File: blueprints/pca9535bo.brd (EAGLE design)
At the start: 160 x 100 mm, 8 parts, among them IC1 PCA9535D, J1 0R, J2 0R, J3 0R

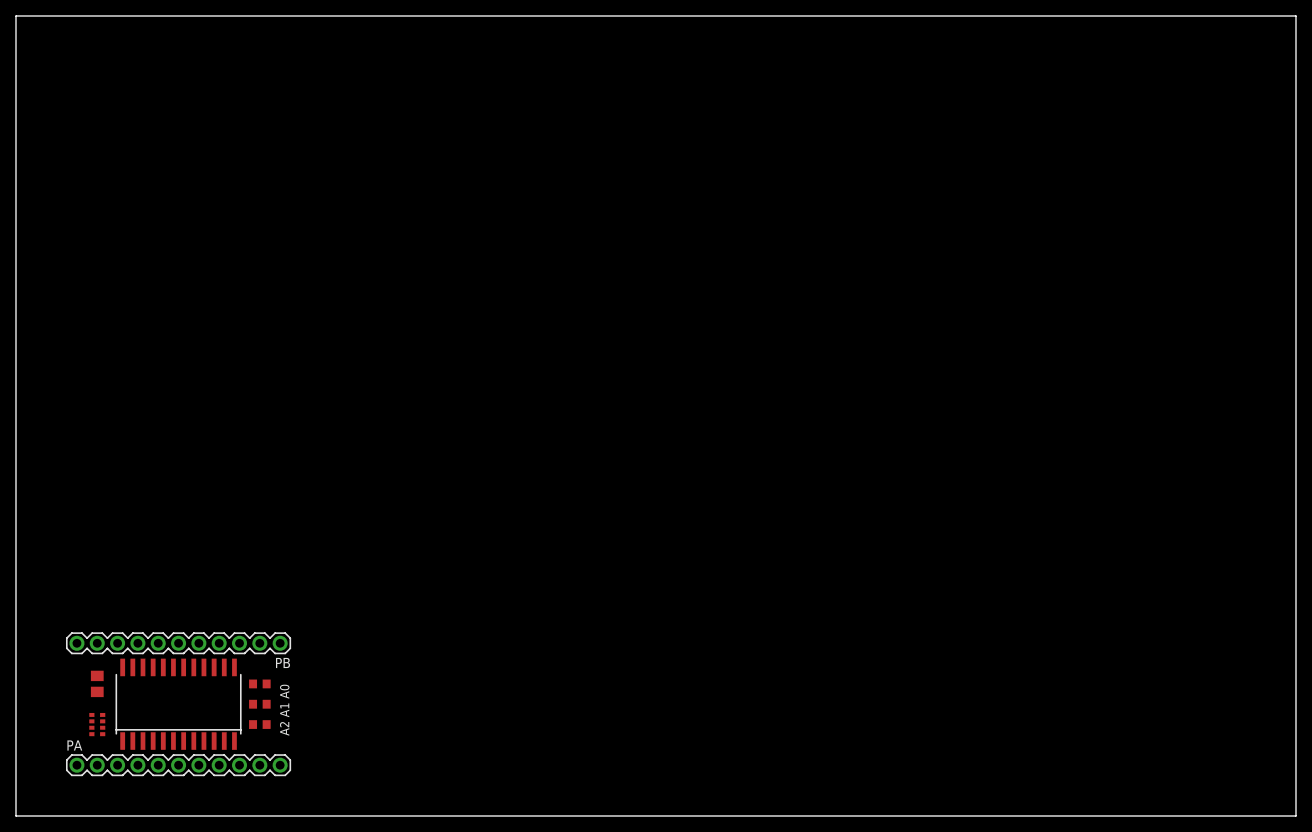
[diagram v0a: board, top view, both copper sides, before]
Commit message: I2C pullups and sizing down
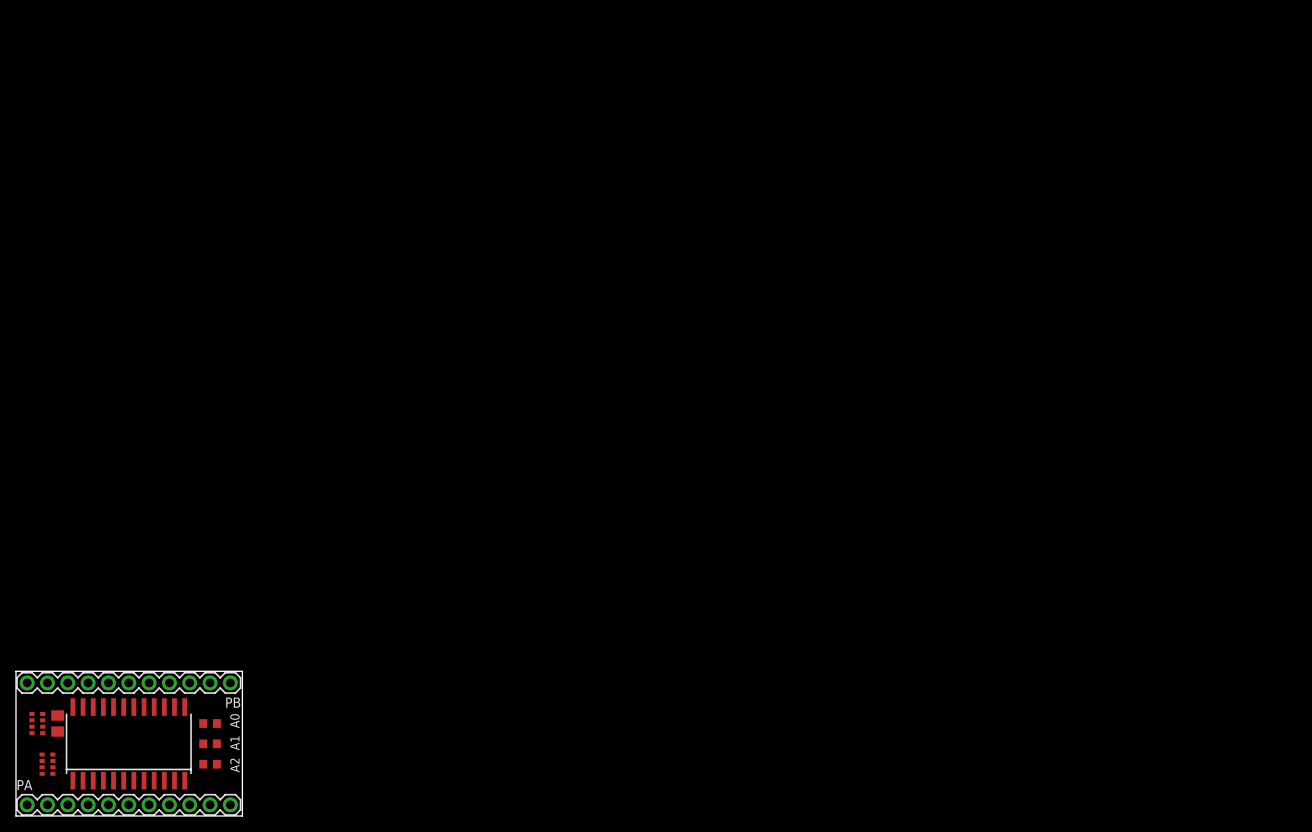
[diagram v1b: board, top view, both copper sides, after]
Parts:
- added PU2: 4.7k, resistor-dil:CAY16
- moved IC1 7.95 mm to (14.1, 9.02)
- moved J1 7.95 mm to (24.3, 11.6)
- moved J3 7.95 mm to (24.3, 9.02)
- moved PB 7.95 mm to (26.8, 16.6)
- moved PA 7.95 mm to (1.40, 1.40)
- moved PU 7.95 mm to (3.94, 6.48)
- moved J2 7.95 mm to (24.3, 6.48)
- moved C1 7.00 mm to (5.21, 11.6)
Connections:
- net 5V: now also PU2.1, PU2.4
- net SCL: now also PU2.5, PU2.6
- net SDA: now also PU2.7, PU2.8
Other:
- board size 160 x 100 mm -> 28.3 x 18.1 mm

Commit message: ground polygons
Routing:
- added copper zone on layer 1, net GND
- added copper zone on layer 16, net GND
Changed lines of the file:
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@@
 <contactref element="IC1" pad="8"/>
 <contactref element="PA" pad="8"/>
-<wire x1="16.002" y1="4.417" x2="19.177" y2="1.397" width="0" layer="19" extent="1-1"/>
+<wire x1="19.177" y1="1.397" x2="16.002" y2="4.417" width="0" layer="19" extent="1-1"/>
 </signal>
 <signal name="PA5">
@@
 <contactref element="IC1" pad="19"/>
 <contactref element="PB" pad="7"/>
-<wire x1="13.462" y1="13.617" x2="11.557" y2="16.637" width="0" layer="19" extent="1-1"/>
+<wire x1="11.557" y1="16.637" x2="13.462" y2="13.617" width="0" layer="19" extent="1-1"/>
 </signal>
 <signal name="PB7">
@@
 <contactref element="PU2" pad="5"/>
 <wire x1="3.937" y1="16.637" x2="9.652" y2="13.617" width="0" layer="19" extent="1-1"/>
-<wire x1="3.342" y1="10.357" x2="9.652" y2="13.617" width="0" layer="19" extent="1-1"/>
-<wire x1="3.342" y1="11.157" x2="3.342" y2="10.357" width="0" layer="19" extent="1-1"/>
+<wire x1="3.342" y1="11.157" x2="3.937" y2="16.637" width="0" layer="19" extent="1-1"/>
+<wire x1="3.342" y1="10.357" x2="3.342" y2="11.157" width="0" layer="19" extent="1-1"/>
 </signal>
 <signal name="SDA">
@@
 <contactref element="PU2" pad="7"/>
 <contactref element="PU2" pad="8"/>
-<wire x1="1.397" y1="16.637" x2="8.382" y2="13.617" width="0" layer="19" extent="1-1"/>
-<wire x1="3.342" y1="11.957" x2="8.382" y2="13.617" width="0" layer="19" extent="1-1"/>
-<wire x1="3.342" y1="12.757" x2="3.342" y2="11.957" width="0" layer="19" extent="1-1"/>
+<wire x1="3.342" y1="12.757" x2="8.382" y2="13.617" width="0" layer="19" extent="1-1"/>
+<wire x1="3.342" y1="11.957" x2="3.342" y2="12.757" width="0" layer="19" extent="1-1"/>
+<wire x1="1.397" y1="16.637" x2="3.342" y2="12.757" width="0" layer="19" extent="1-1"/>
 </signal>
 <signal name="5V">
@@
 <contactref element="PU2" pad="4"/>
 <wire x1="5.207" y1="12.557" x2="7.112" y2="13.617" width="0" layer="19" extent="1-1"/>
-<wire x1="3.262" y1="7.677" x2="5.207" y2="12.557" width="0" layer="19" extent="1-1"/>
+<wire x1="1.992" y1="12.757" x2="5.207" y2="12.557" width="0" layer="19" extent="1-1"/>
+<wire x1="1.992" y1="10.357" x2="1.992" y2="12.757" width="0" layer="19" extent="1-1"/>
+<wire x1="3.262" y1="7.677" x2="1.992" y2="10.357" width="0" layer="19" extent="1-1"/>
 <wire x1="3.262" y1="6.877" x2="3.262" y2="7.677" width="0" layer="19" extent="1-1"/>
 <wire x1="3.262" y1="6.077" x2="3.262" y2="6.877" width="0" layer="19" extent="1-1"/>
 <wire x1="3.262" y1="5.277" x2="3.262" y2="6.077" width="0" layer="19" extent="1-1"/>
 <wire x1="3.937" y1="1.397" x2="3.262" y2="5.277" width="0" layer="19" extent="1-1"/>
-<wire x1="1.992" y1="10.357" x2="3.937" y2="1.397" width="0" layer="19" extent="1-1"/>
-<wire x1="1.992" y1="12.757" x2="1.992" y2="10.357" width="0" layer="19" extent="1-1"/>
 </signal>
 <signal name="GND">
@@
 <contactref element="J2" pad="2"/>
 <contactref element="J3" pad="2"/>
-<wire x1="25.107" y1="9.017" x2="25.107" y2="11.557" width="0" layer="19" extent="1-1"/>
-<wire x1="25.107" y1="6.477" x2="25.107" y2="9.017" width="0" layer="19" extent="1-1"/>
-<wire x1="21.082" y1="4.417" x2="25.107" y2="6.477" width="0" layer="19" extent="1-1"/>
-<wire x1="5.207" y1="10.557" x2="21.082" y2="4.417" width="0" layer="19" extent="1-1"/>
-<wire x1="1.397" y1="1.397" x2="5.207" y2="10.557" width="0" layer="19" extent="1-1"/>
+<polygon width="0.254" layer="16" spacing="0.254" isolate="0.254">
+<vertex x="0" y="18.034"/>
+<vertex x="0" y="0"/>
+<vertex x="28.321" y="0"/>
+<vertex x="28.321" y="18.161"/>
+<vertex x="0" y="18.161"/>
+</polygon>
+<polygon width="0.254" layer="1" spacing="0.254" isolate="0.254">
+<vertex x="0" y="18.034"/>
+<vertex x="0" y="0"/>
+<vertex x="28.321" y="0"/>
+<vertex x="28.321" y="18.034"/>
+</polygon>
 </signal>
 <signal name="A1">

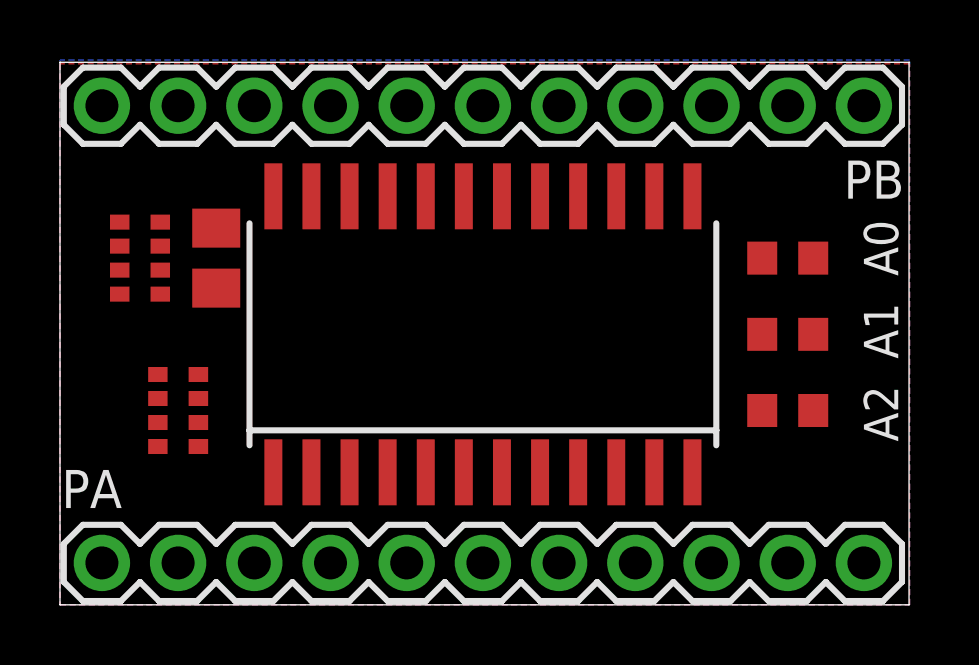
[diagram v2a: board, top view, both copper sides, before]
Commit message: two polygons at least was a bad idea
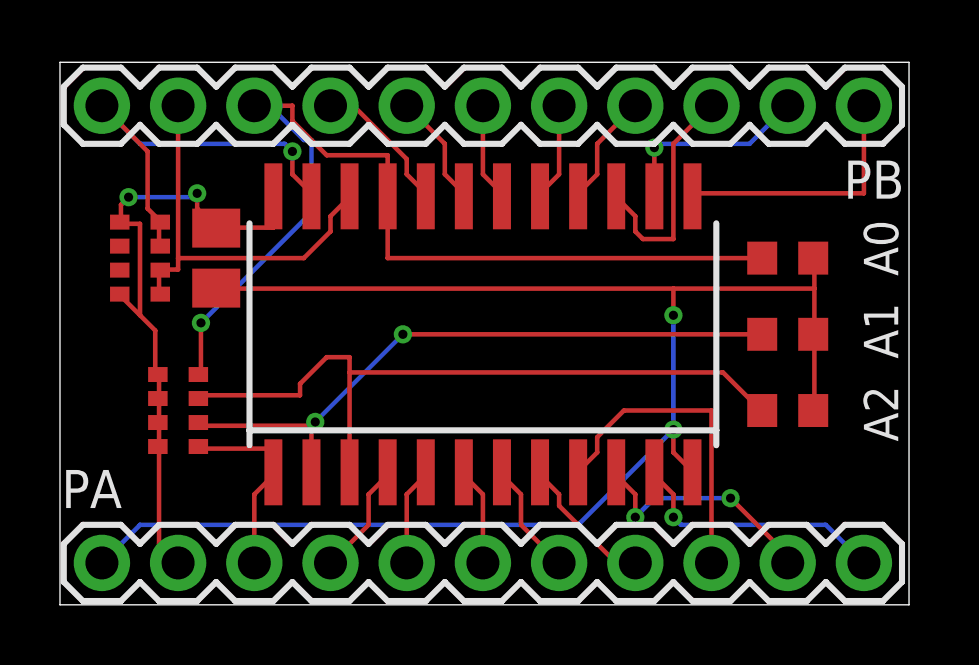
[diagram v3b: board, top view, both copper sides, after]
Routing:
- net GND: track 0.00 -> 52.4 mm, vias 0 -> 2
- net A0: track 0.00 -> 33.1 mm, vias 0 -> 1
- net A2: track 0.00 -> 24.0 mm
- net A1: track 0.00 -> 21.7 mm, vias 0 -> 2
- net 5V: track 0.00 -> 21.3 mm, vias 0 -> 2
- net SDA: track 0.00 -> 14.2 mm, vias 0 -> 1
- net SCL: track 0.00 -> 13.8 mm
- net PA5: track 0.00 -> 10.7 mm
- net PA7: track 0.00 -> 8.74 mm, vias 0 -> 1
- net PB0: track 0.00 -> 8.73 mm
- net PA6: track 0.00 -> 8.15 mm, vias 0 -> 2
- net PB2: track 0.00 -> 7.78 mm
- net PB1: track 0.00 -> 6.65 mm, vias 0 -> 1
- net INT-: track 0.00 -> 6.60 mm
- net PB7: track 0.00 -> 4.78 mm
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- removed copper zone on layer 1, net GND
- removed copper zone on layer 16, net GND

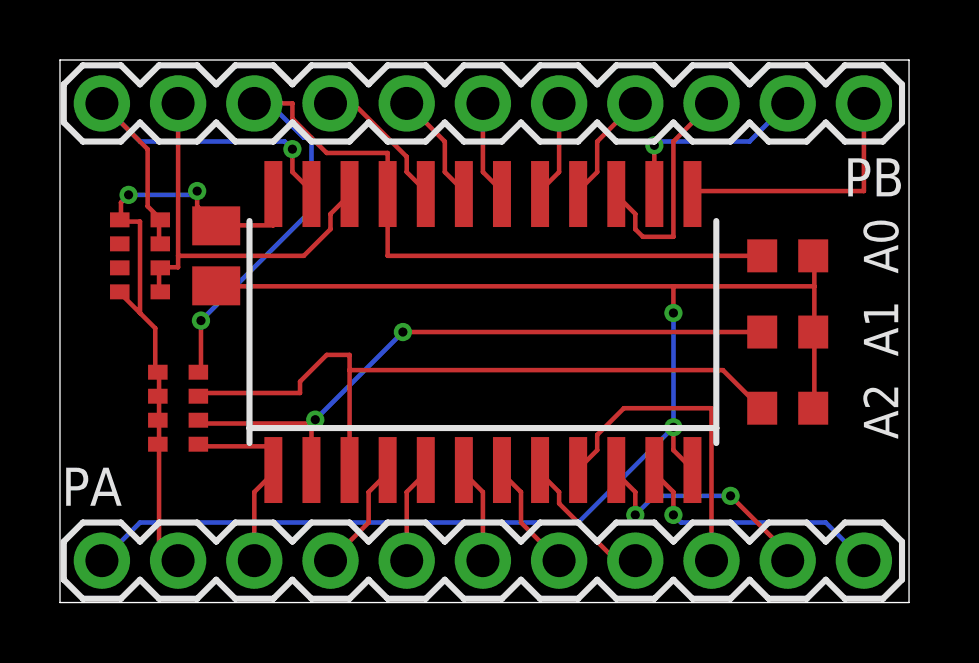
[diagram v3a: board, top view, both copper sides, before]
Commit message: 10mil traces seem to route just fine so use them
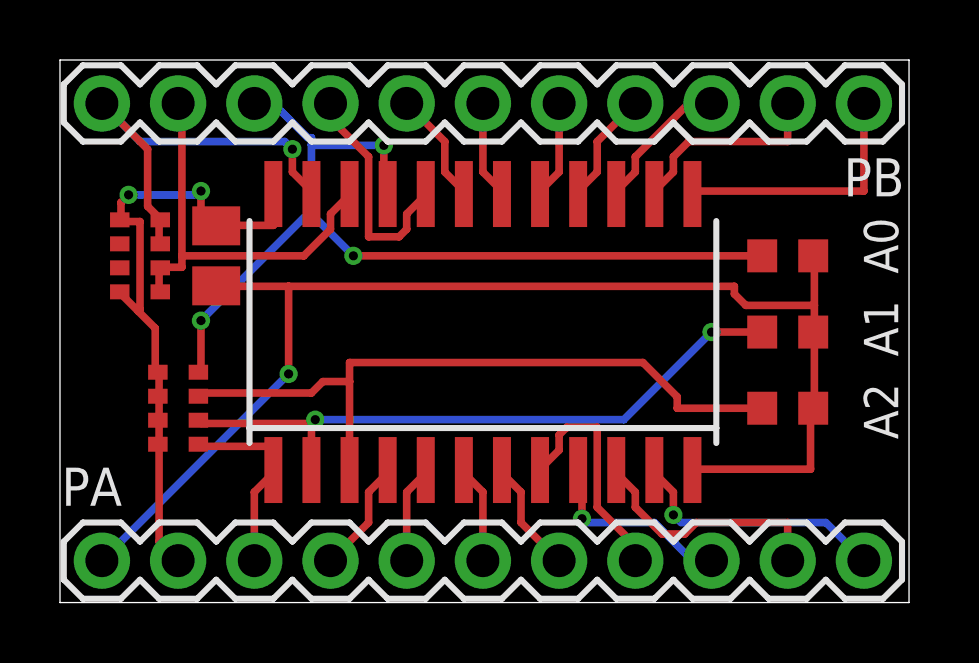
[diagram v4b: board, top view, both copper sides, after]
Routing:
- net GND: track 52.4 -> 43.4 mm, vias 2 -> 1
- net PA5: track 10.7 -> 6.57 mm, vias 0 -> 1
- net PA4: track 4.71 -> 7.78 mm
- net PB7: track 4.78 -> 7.78 mm
- net PB2: track 7.78 -> 4.78 mm
- net A0: track 33.1 -> 31.5 mm, vias 1 -> 3
- net A2: track 24.0 -> 23.4 mm
- net PA6: track 8.15 -> 8.38 mm, vias 2 -> 0
- net PB1: track 6.65 -> 6.80 mm, vias 1 -> 0

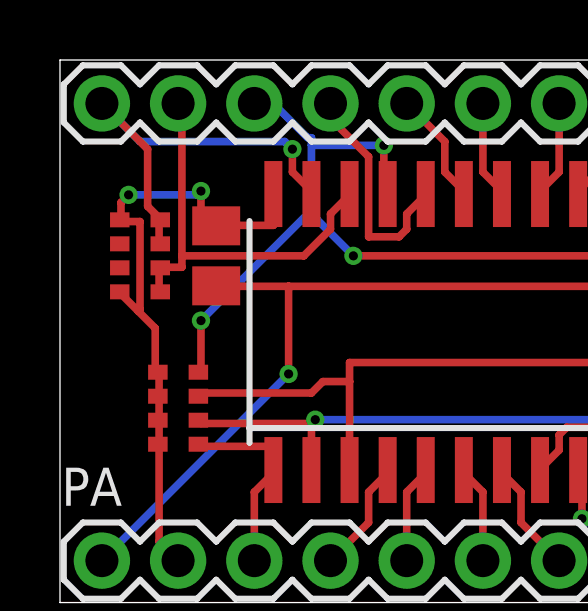
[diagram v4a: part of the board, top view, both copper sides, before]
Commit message: forgot some junction
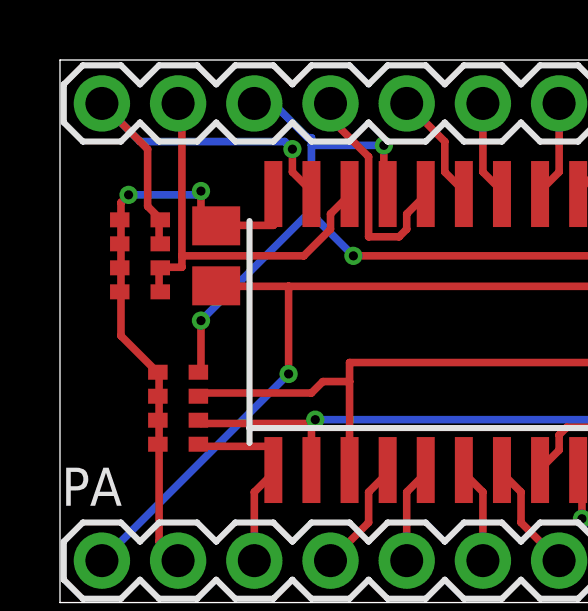
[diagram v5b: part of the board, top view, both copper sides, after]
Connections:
- net 5V: now also PU2.2, PU2.3
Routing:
- net 5V: track 21.3 -> 20.1 mm
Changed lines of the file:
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@@
 <contactref element="PU2" pad="1"/>
 <contactref element="PU2" pad="4"/>
+<contactref element="PU2" pad="3"/>
+<contactref element="PU2" pad="2"/>
 <wire x1="7.112" y1="12.573" x2="5.207" y2="12.573" width="0.254" layer="1"/>
 <wire x1="7.112" y1="13.617" x2="7.112" y2="12.573" width="0.254" layer="1"/>
@@
 <wire x1="3.302" y1="6.985" x2="3.262" y2="6.877" width="0.254" layer="1"/>
 <wire x1="3.302" y1="7.62" x2="3.262" y2="7.677" width="0.254" layer="1"/>
-<wire x1="3.175" y1="9.144" x2="2.6035" y2="9.7155" width="0.254" layer="1"/>
-<wire x1="2.6035" y1="9.7155" x2="2.032" y2="10.287" width="0.254" layer="1"/>
-<wire x1="3.175" y1="7.747" x2="3.175" y2="9.144" width="0.254" layer="1"/>
-<wire x1="2.032" y1="10.287" x2="1.992" y2="10.357" width="0.254" layer="1"/>
-<wire x1="3.175" y1="7.747" x2="3.262" y2="7.677" width="0.254" layer="1"/>
-<wire x1="2.667" y1="12.7" x2="2.032" y2="12.7" width="0.254" layer="1"/>
-<wire x1="2.667" y1="9.779" x2="2.667" y2="12.7" width="0.254" layer="1"/>
-<wire x1="2.032" y1="12.7" x2="1.992" y2="12.757" width="0.254" layer="1"/>
-<wire x1="2.667" y1="9.779" x2="2.6035" y2="9.7155" width="0.254" layer="1"/>
 <wire x1="3.302" y1="6.858" x2="3.302" y2="6.096" width="0.254" layer="1"/>
 <wire x1="3.302" y1="6.096" x2="3.262" y2="6.077" width="0.254" layer="1"/>
 <wire x1="3.302" y1="6.858" x2="3.262" y2="6.877" width="0.254" layer="1"/>
+<wire x1="2.032" y1="11.049" x2="2.032" y2="10.414" width="0.254" layer="1"/>
+<wire x1="2.032" y1="10.414" x2="1.992" y2="10.357" width="0.254" layer="1"/>
+<wire x1="2.032" y1="11.049" x2="1.992" y2="11.157" width="0.254" layer="1"/>
+<wire x1="2.032" y1="12.7" x2="2.032" y2="12.065" width="0.254" layer="1"/>
+<wire x1="2.032" y1="12.065" x2="1.992" y2="11.957" width="0.254" layer="1"/>
+<wire x1="2.032" y1="12.7" x2="1.992" y2="12.757" width="0.254" layer="1"/>
+<wire x1="2.032" y1="11.938" x2="2.032" y2="11.176" width="0.254" layer="1"/>
+<wire x1="2.032" y1="11.176" x2="1.992" y2="11.157" width="0.254" layer="1"/>
+<wire x1="2.032" y1="11.938" x2="1.992" y2="11.957" width="0.254" layer="1"/>
+<wire x1="2.032" y1="8.89" x2="3.175" y2="7.747" width="0.254" layer="1"/>
+<wire x1="2.032" y1="10.287" x2="2.032" y2="8.89" width="0.254" layer="1"/>
+<wire x1="3.175" y1="7.747" x2="3.262" y2="7.677" width="0.254" layer="1"/>
+<wire x1="2.032" y1="10.287" x2="1.992" y2="10.357" width="0.254" layer="1"/>
 <wire x1="4.699" y1="13.081" x2="5.207" y2="12.573" width="0.254" layer="1"/>
 <wire x1="4.699" y1="13.716" x2="4.699" y2="13.081" width="0.254" layer="1"/>
